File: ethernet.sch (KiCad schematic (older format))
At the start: 46 parts, among them U11 KSZ9031RNXCA, Y1 ABM8G-25.000MHZ-18-D2Y-T

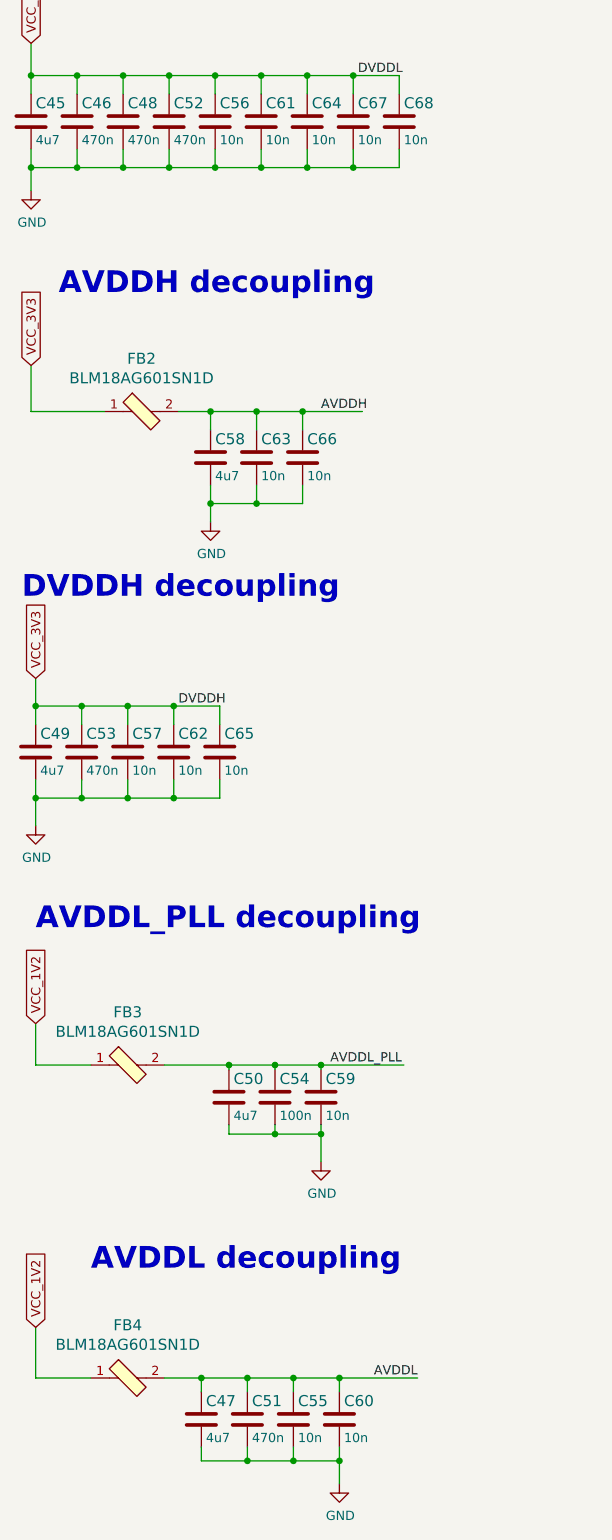
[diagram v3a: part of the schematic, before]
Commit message: Updated component placement - PHY passives placed, moved HDMI IC, lowered VIC and DDRs
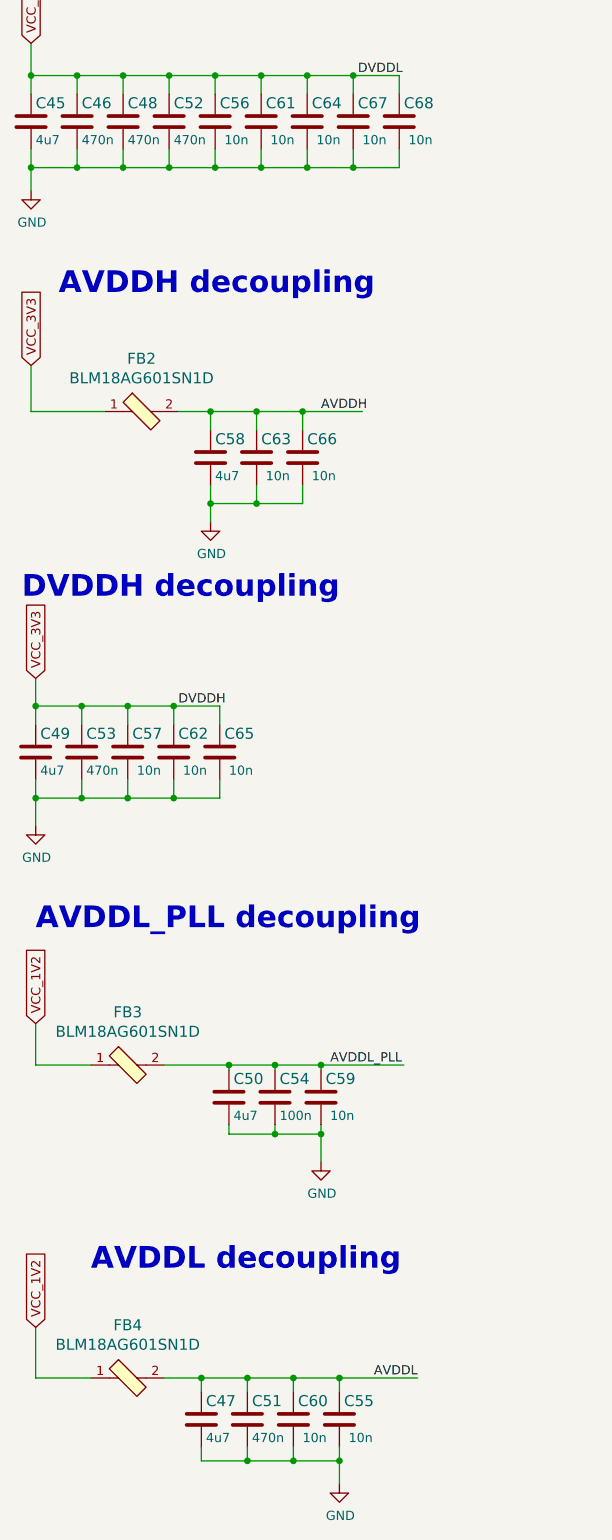
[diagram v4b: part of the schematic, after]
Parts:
- removed C46, C48, C51, C52, C53: C_470n_0402, arvsom-footprints:0402-cap, symbol arvsom:C_470n_0402
- removed C54: C_100n_0402, arvsom-footprints:0402-cap, symbol arvsom:C_100n_0402
- removed C55, C56, C57, C59, C60, C61, C62, C63, C64, C65, C66, C67, C68: C_10n_0402, arvsom-footprints:0402-cap, symbol arvsom:C_10n_0402
- removed R31, R32, R33, R34, R35, R36, R38, R39, R40: R_10k_0402, arvsom-footprints:0402-res, symbol arvsom:R_10k_0402
- added C46, C48, C51, C52, C53: C_470n_0201, arvsom-footprints:0201-res, symbol arvsom:C_470n_0201
- added C54: C_100n_0201, arvsom-footprints:0201-res, symbol arvsom:C_100n_0201
- added C55, C56, C57, C59, C60, C61, C62, C63, C64, C65, C66, C67, C68: C_10n_0201, arvsom-footprints:0201-res, symbol arvsom:C_10n_0201
- added R31, R32, R33, R34, R35, R36, R38, R39, R40: R_10k_0201, arvsom-footprints:0201-res, symbol arvsom:R_10k_0201
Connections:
- net AVDDH: now also C63.1, C66.1
- net AVDDL: now also C51.1, C55.1, C60.1
- net AVDDL_PLL: now also C54.1, C59.1
- net ETH_LED1: now also R40.1
- net ETH_LED2: now also R39.1
- net GND: now also C46.2, C48.2, C51.2, C52.2, C53.2, C54.2, C55.2, C56.2, C57.2, C59.2, C60.2, C61.2, C62.2, C63.2, C64.2, C65.2, C66.2, C67.2, C68.2
- net LED_MODE: now also R36.1
- net RGMII_MDC: now also R38.1
- net RGMII_RXCLK: now also R35.1
- net RGMII_RXD0: now also R31.1
- net RGMII_RXD1: now also R32.1
- net RGMII_RXD2: now also R33.1
- net RGMII_RXD3: now also R34.1
- net VCC_1V2: now also C46.1, C48.1, C52.1, C56.1, C61.1, C64.1, C67.1, C68.1
- net VCC_3V3: now also C53.1, C57.1, C62.1, C65.1, R31.2, R32.2, R33.2, R34.2, R35.2, R36.2, R38.2, R39.2, R40.2

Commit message: Finished component placement
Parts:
- removed R46, R47: R_0R_0402, arvsom-footprints:0402-res, symbol arvsom:R_0R_0402
- added R46, R47: R_0R_0201, arvsom-footprints:0201-res, symbol arvsom:R_0R_0201
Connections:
- net ETH_RESETn: now also R46.2, R47.2
- net GPIO63_GMAC_RESETN: now also R47.1
- net SYS_RSTN: now also R46.1
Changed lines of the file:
@@
 Text GLabel 7875 5800 0    50   Input ~ 0
 SYS_RSTN
-$Comp
-L arvsom:R_0R_0402 R?
-U 1 1 60990FCF
-P 8100 5800
-AR Path="/60751C8D/60990FCF" Ref="R?"  Part="1"
-AR Path="/60980C6E/60990FCF" Ref="R46"  Part="1"
-F 0 "R46" H 7925 5850 60  0000 C CNN
-F 1 "R_0R_0402" H 8100 5650 60  0001 C CNN
-F 2 "arvsom-footprints:0402-res" H 8300 6000 60  0001 L CNN
-F 3 "" H 8100 5800 50  0001 C CNN
-F 4 "PANASONIC" H 8300 6200 60  0001 L CNN "Manufacturer"
-F 5 "ERJ2GE0R00X" H 8300 6100 60  0001 L CNN "MPN"
-F 6 "0R" H 8250 5850 50  0000 C CNN "Val"
-	1    8100 5800
-	1    0    0    -1
-$EndComp
 Text GLabel 7900 5950 0    50   Input ~ 0
 GPIO63_GMAC_RESETN
-$Comp
-L arvsom:R_0R_0402 R?
-U 1 1 609C4F31
-P 8100 5950
-AR Path="/60751C8D/609C4F31" Ref="R?"  Part="1"
-AR Path="/60980C6E/609C4F31" Ref="R47"  Part="1"
-F 0 "R47" H 7925 6000 60  0000 C CNN
-F 1 "R_0R_0402" H 8100 5800 60  0001 C CNN
-F 2 "arvsom-footprints:0402-res" H 8300 6150 60  0001 L CNN
-F 3 "" H 8100 5950 50  0001 C CNN
-F 4 "PANASONIC" H 8300 6350 60  0001 L CNN "Manufacturer"
-F 5 "ERJ2GE0R00X" H 8300 6250 60  0001 L CNN "MPN"
-F 6 "0R" H 8250 6000 50  0000 C CNN "Val"
-F 7 "DNP" H 8100 5950 50  0000 C CNN "DNP"
-	1    8100 5950
-	1    0    0    -1
-$EndComp
 Wire Wire Line
 	8700 5800 8525 5800
@@
 	1    0    0    -1
 $EndComp
+$Comp
+L arvsom:R_0R_0201 R46
+U 1 1 61F72BFE
+P 8100 5800
+F 0 "R46" H 7925 5850 60  0000 C CNN
+F 1 "R_0R_0201" H 8100 5650 60  0001 C CNN
+F 2 "arvsom-footprints:0201-res" H 8300 6000 60  0001 L CNN
+F 3 "" H 8100 5800 50  0001 C CNN
+F 4 "Vishay" H 8300 6200 60  0001 L CNN "Manufacturer"
+F 5 "CRCW02010000Z0ED" H 8300 6100 60  0001 L CNN "MPN"
+F 6 "0R" H 8250 5850 50  0000 C CNN "Val"
+	1    8100 5800
+	1    0    0    -1
+$EndComp
+$Comp
+L arvsom:R_0R_0201 R47
+U 1 1 61F74222
+P 8100 5950
+F 0 "R47" H 7925 6000 60  0000 C CNN
+F 1 "R_0R_0201" H 8100 5800 60  0001 C CNN
+F 2 "arvsom-footprints:0201-res" H 8300 6150 60  0001 L CNN
+F 3 "" H 8100 5950 50  0001 C CNN
+F 4 "Vishay" H 8300 6350 60  0001 L CNN "Manufacturer"
+F 5 "CRCW02010000Z0ED" H 8300 6250 60  0001 L CNN "MPN"
+F 6 "0R" H 8250 6000 50  0000 C CNN "Val"
+F 7 "DNP" H 8100 5950 50  0000 C CNN "Populate"
+	1    8100 5950
+	1    0    0    -1
+$EndComp
